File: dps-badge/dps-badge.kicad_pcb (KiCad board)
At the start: 2 copper layers, 39.3 x 41.1 mm, 12 parts, among them SW0 SW_SPDT

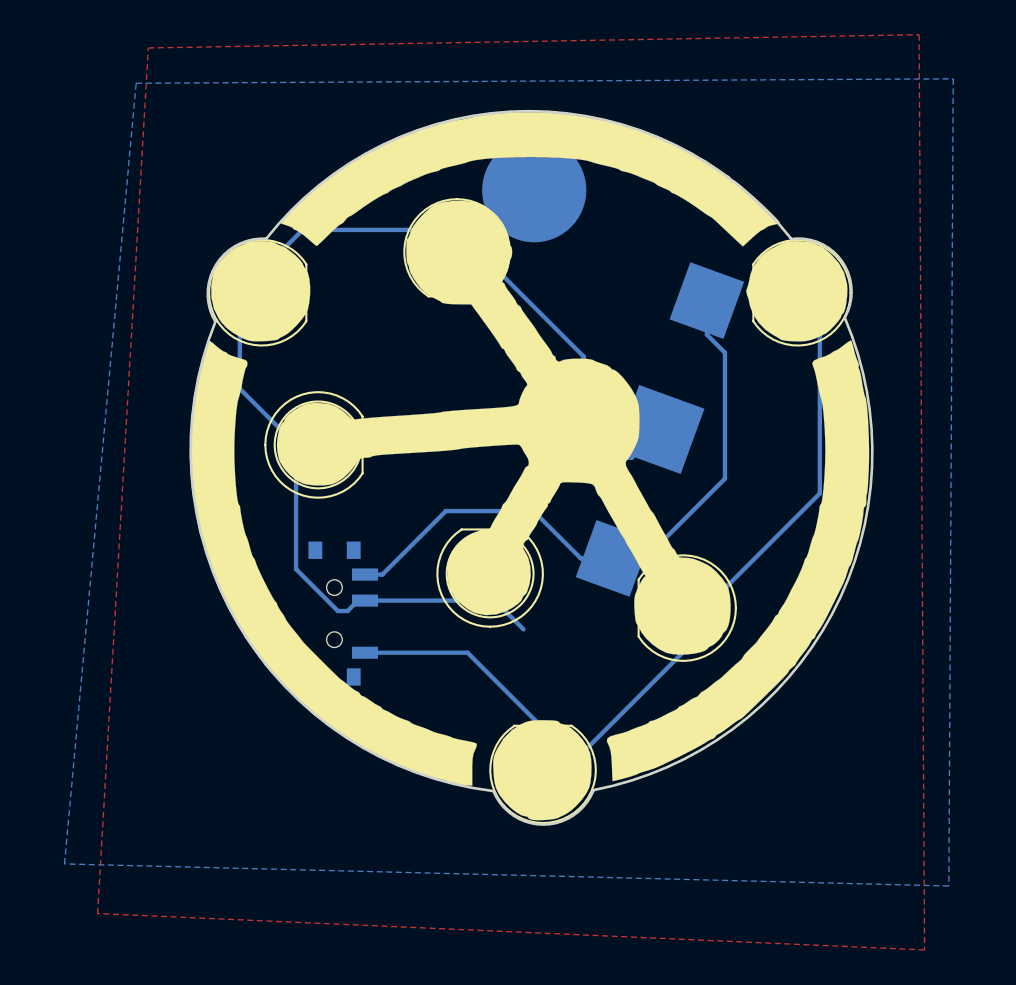
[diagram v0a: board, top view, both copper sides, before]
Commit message: basic code for neopixel clock + adjustments to dps badge + chronodot lib + nixie clock base
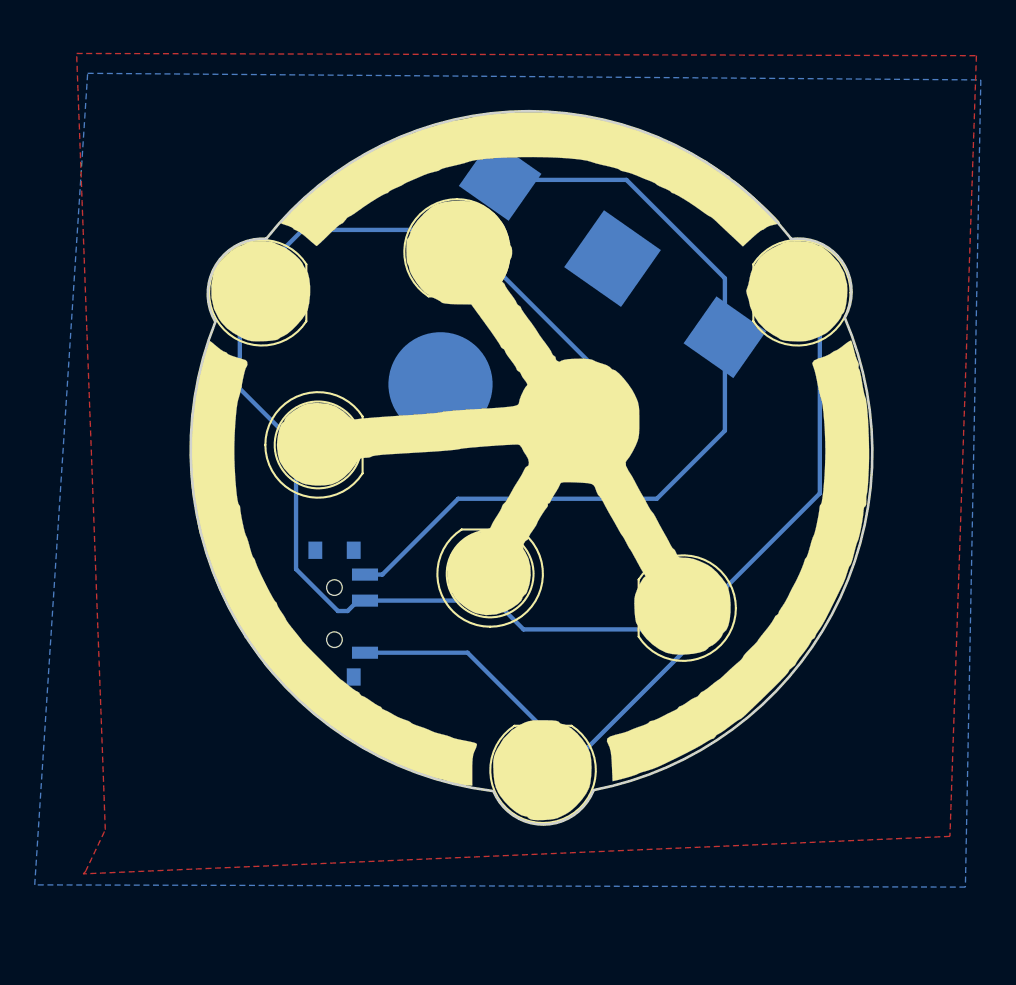
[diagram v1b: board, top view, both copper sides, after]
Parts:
- moved REF** 12.4 mm to (186.1, 97.3)
- moved BT0 10.2 mm to (196.0, 90.0), turned to 325 degrees
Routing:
- net Net-(BT0-Pad1): track 36.0 -> 48.2 mm
- net Net-(D0-Pad2): track 96.7 -> 106.0 mm
- net GND: track 21.5 -> 13.2 mm
- added copper zone on B.Cu, net GND
- removed copper zone on B.Cu, net Net-(D0-Pad2)
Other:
- board text added: "Azure IoT Hub Device Provisioning Service @pierreca v1.1"
- board text removed: "DPS @pierreca v1.0"
